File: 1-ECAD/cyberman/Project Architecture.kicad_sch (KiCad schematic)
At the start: 0 parts

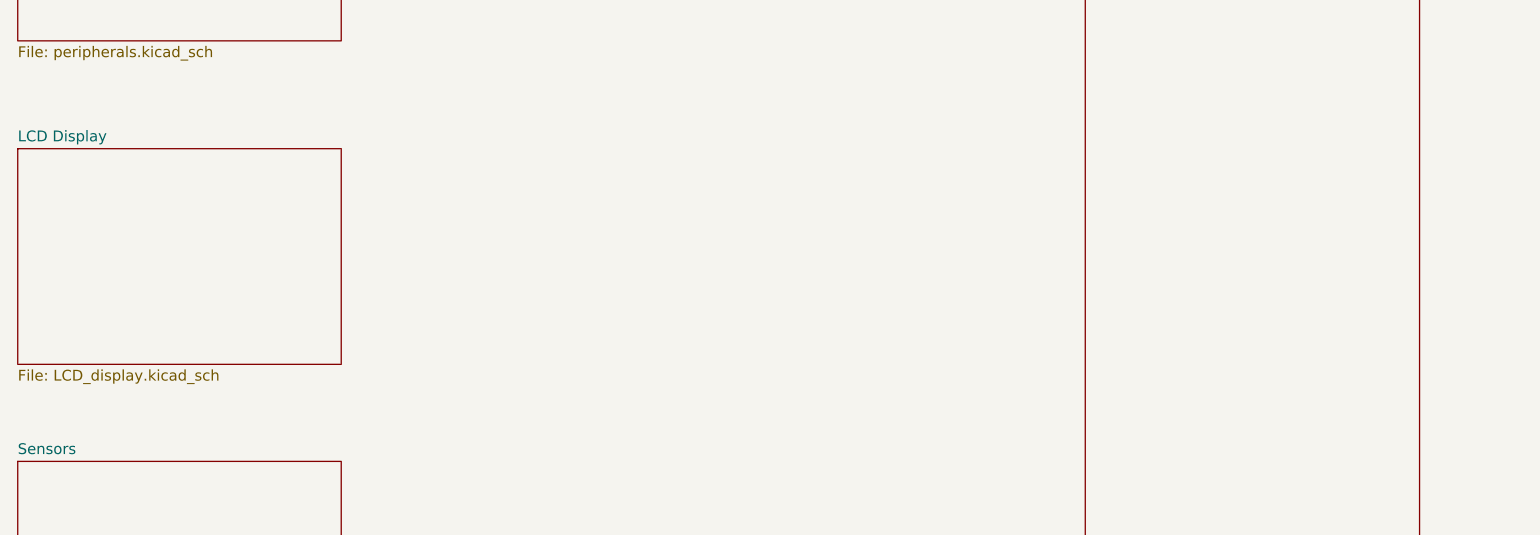
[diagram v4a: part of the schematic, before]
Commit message: add bus and display connection
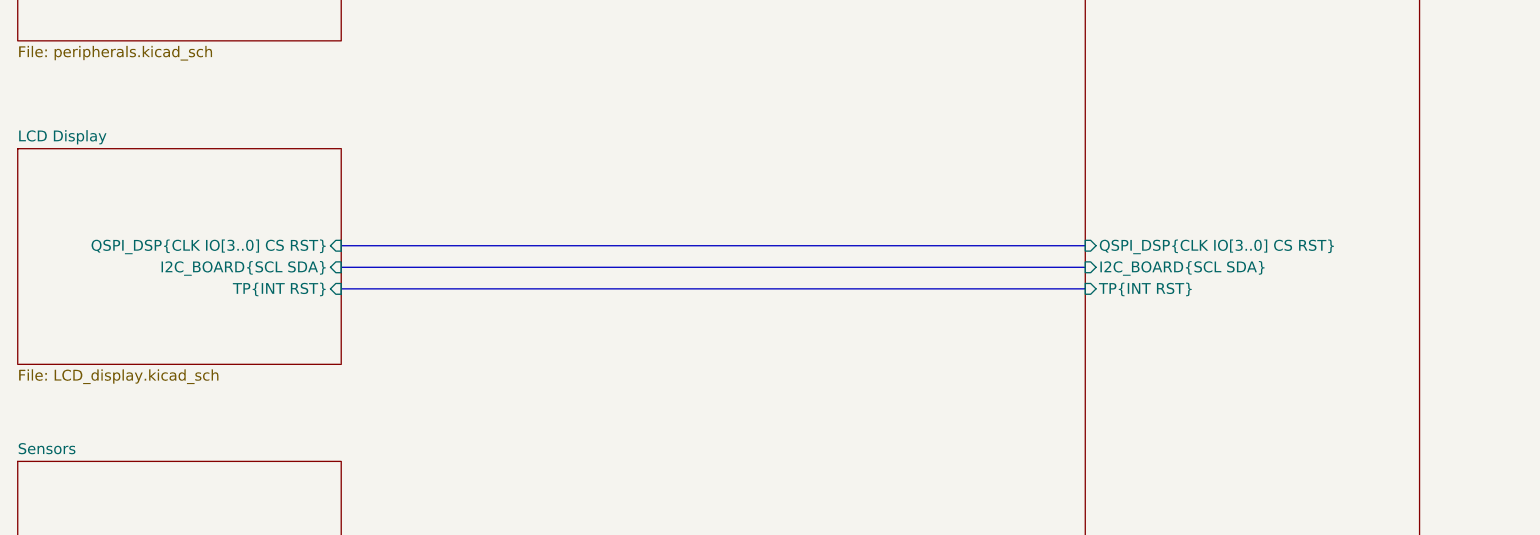
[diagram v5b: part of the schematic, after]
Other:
- sheet LCD Display ports: added I2C_BOARD{SCL SDA}, QSPI_DSP{CLK IO[3..0] CS RST}, TP{INT RST}; removed none
- sheet MCU - IOs ports: added I2C_BOARD{SCL SDA}, QSPI_DSP{CLK IO[3..0] CS RST}, TP{INT RST}; removed none
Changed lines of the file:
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@@
 		(company "${COMPANY}")
+	)
+	(bus
+		(pts
+			(xy 127 138.43) (xy 214.63 138.43)
+		)
+		(stroke
+			(width 0)
+			(type default)
+		)
+	)
+	(bus
+		(pts
+			(xy 127 140.97) (xy 214.63 140.97)
+		)
+		(stroke
+			(width 0)
+			(type default)
+		)
+	)
+	(bus
+		(pts
+			(xy 127 143.51) (xy 214.63 143.51)
+		)
+		(stroke
+			(width 0)
+			(type default)
+		)
 	)
 	(text_box "[${#}] ${TITLE}"
@@
 			)
 		)
+		(pin "QSPI_DSP{CLK IO[3..0] CS RST}" input
+			(at 127 138.43 0)
+			(effects
+				(font
+					(size 1.27 1.27)
+				)
+				(justify right)
+			)
+		)
+		(pin "TP{INT RST}" input
+			(at 127 143.51 0)
+			(effects
+				(font
+					(size 1.27 1.27)
+				)
+				(justify right)
+			)
+		)
+		(pin "I2C_BOARD{SCL SDA}" input
+			(at 127 140.97 0)
+			(effects
+				(font
+					(size 1.27 1.27)
+				)
+				(justify right)
+			)
+		)
 		(instances
 			(project "cyberman"
@@
 			)
 		)
+		(pin "TP{INT RST}" input
+			(at 214.63 143.51 180)
+			(effects
+				(font
+					(size 1.27 1.27)
+				)
+				(justify left)
+			)
+		)
+		(pin "QSPI_DSP{CLK IO[3..0] CS RST}" input
+			(at 214.63 138.43 180)
+			(effects
+				(font
+					(size 1.27 1.27)
+				)
+				(justify left)
+			)
+		)
+		(pin "I2C_BOARD{SCL SDA}" input
+			(at 214.63 140.97 180)
+			(effects
+				(font
+					(size 1.27 1.27)
+				)
+				(justify left)
+			)
+		)

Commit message: hey
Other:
- sheet LCD Display ports: added BOARD_I2C{SCL SDA}, DSP{CS RST}, QSPI{CLK IO[3..0]}; removed I2C_BOARD{SCL SDA}, QSPI_DSP{CLK IO[3..0] CS RST}
- sheet MCU - IOs ports: added BOARD_I2C{SCL SDA}, DSP{CS RST}, I2S{SCK SD WS}, QSPI{CLK IO[3..0]}, SD{CS CD}; removed I2C_BOARD{SCL SDA}, QSPI_DSP{CLK IO[3..0] CS RST}
- sheet Peripherals ports: added QSPI{CLK IO[3..0]}, SD{CS CD}; removed none
- sheet Power ports: added I2C_AUX{SCL SDA}, I2C_BOARD{SCL SDA}, PWR{PERIPH RST}; removed none
- sheet Sensors ports: added I2C_BOARD{SCL SDA}, I2S{SCK SD WS}; removed none
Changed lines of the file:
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@@
 		(company "${COMPANY}")
 	)
-	(bus
-		(pts
-			(xy 127 138.43) (xy 214.63 138.43)
-		)
-		(stroke
-			(width 0)
-			(type default)
-		)
-	)
-	(bus
-		(pts
-			(xy 127 140.97) (xy 214.63 140.97)
-		)
-		(stroke
-			(width 0)
-			(type default)
-		)
-	)
-	(bus
-		(pts
-			(xy 127 143.51) (xy 214.63 143.51)
+	(junction
+		(at 163.83 142.24)
+		(diameter 0)
+		(color 0 0 0 0)
+	)
+	(junction
+		(at 163.83 134.62)
+		(diameter 0)
+		(color 0 0 0 0)
+	)
+	(bus
+		(pts
+			(xy 127 179.07) (xy 214.63 179.07)
+		)
+		(stroke
+			(width 0)
+			(type default)
+		)
+	)
+	(bus
+		(pts
+			(xy 163.83 99.06) (xy 163.83 134.62)
+		)
+		(stroke
+			(width 0)
+			(type default)
+		)
+	)
+	(bus
+		(pts
+			(xy 127 139.7) (xy 214.63 139.7)
+		)
+		(stroke
+			(width 0)
+			(type default)
+		)
+	)
+	(bus
+		(pts
+			(xy 127 99.06) (xy 163.83 99.06)
+		)
+		(stroke
+			(width 0)
+			(type default)
+		)
+	)
+	(bus
+		(pts
+			(xy 127 134.62) (xy 163.83 134.62)
+		)
+		(stroke
+			(width 0)
+			(type default)
+		)
+	)
+	(bus
+		(pts
+			(xy 127 142.24) (xy 163.83 142.24)
+		)
+		(stroke
+			(width 0)
+			(type default)
+		)
+	)
+	(bus
+		(pts
+			(xy 127 101.6) (xy 214.63 101.6)
+		)
+		(stroke
+			(width 0)
+			(type default)
+		)
+	)
+	(bus
+		(pts
+			(xy 163.83 142.24) (xy 214.63 142.24)
+		)
+		(stroke
+			(width 0)
+			(type default)
+		)
+	)
+	(bus
+		(pts
+			(xy 163.83 134.62) (xy 214.63 134.62)
+		)
+		(stroke
+			(width 0)
+			(type default)
+		)
+	)
+	(bus
+		(pts
+			(xy 127 176.53) (xy 163.83 176.53)
+		)
+		(stroke
+			(width 0)
+			(type default)
+		)
+	)
+	(bus
+		(pts
+			(xy 163.83 142.24) (xy 163.83 176.53)
+		)
+		(stroke
+			(width 0)
+			(type default)
+		)
+	)
+	(bus
+		(pts
+			(xy 127 137.16) (xy 214.63 137.16)
 		)
 		(stroke
@@
 			)
 		)
+		(pin "I2C_BOARD{SCL SDA}" input
+			(at 127 66.04 0)
+			(effects
+				(font
+					(size 1.27 1.27)
+				)
+				(justify right)
+			)
+		)
+		(pin "I2C_AUX{SCL SDA}" input
+			(at 127 63.5 0)
+			(effects
+				(font
+					(size 1.27 1.27)
+				)
+				(justify right)
+			)
+		)
+		(pin "PWR{PERIPH RST}" input
+			(at 127 60.96 0)
+			(effects
+				(font
+					(size 1.27 1.27)
+				)
+				(justify right)
+			)
+		)
 		(instances
 			(project "cyberman"
@@
 			)
 		)
-		(pin "QSPI_DSP{CLK IO[3..0] CS RST}" input
-			(at 127 138.43 0)
-			(effects
-				(font
-					(size 1.27 1.27)
-				)
-				(justify right)
-			)
-		)
 		(pin "TP{INT RST}" input
-			(at 127 143.51 0)
-			(effects
-				(font
-					(size 1.27 1.27)
-				)
-				(justify right)
-			)
-		)
-		(pin "I2C_BOARD{SCL SDA}" input
-			(at 127 140.97 0)
+			(at 127 139.7 0)
+			(effects
+				(font
+					(size 1.27 1.27)
+				)
+				(justify right)
+			)
+		)
+		(pin "BOARD_I2C{SCL SDA}" input
+			(at 127 142.24 0)
+			(effects
+				(font
+					(size 1.27 1.27)
+				)
+				(justify right)
+			)
+		)
+		(pin "DSP{CS RST}" input
+			(at 127 137.16 0)
+			(effects
+				(font
+					(size 1.27 1.27)
+				)
+				(justify right)
+			)
+		)
+		(pin "QSPI{CLK IO[3..0]}" input
+			(at 127 134.62 0)
 			(effects
 				(font
@@
 			)
 		)
+		(pin "QSPI{CLK IO[3..0]}" input
+			(at 127 99.06 0)
+			(effects
+				(font
+					(size 1.27 1.27)
+				)
+				(justify right)
+			)
+		)
+		(pin "SD{CS CD}" input
+			(at 127 101.6 0)
+			(effects
+				(font
+					(size 1.27 1.27)
+				)
+				(justify right)
+			)
+		)
 		(instances
 			(project "cyberman"
@@
 	)
 	(sheet
-		(at 88.9 163.83)
-		(size 38.1 26.67)
+		(at 88.9 165.1)
+		(size 38.1 25.4)
 		(fields_autoplaced yes)
 		(stroke
@@
 		)
 		(property "Sheetname" "Sensors"
-			(at 88.9 163.1184 0)
+			(at 88.9 164.3884 0)
 			(effects
 				(font
@@
 				)
 				(justify left top)
+			)
+		)
+		(pin "I2C_BOARD{SCL SDA}" input
+			(at 127 176.53 0)
+			(effects
+				(font
+					(size 1.27 1.27)
+				)
+				(justify right)
+			)
+		)
+		(pin "I2S{SCK SD WS}" input
+			(at 127 179.07 0)
+			(effects
+				(font
+					(size 1.27 1.27)
+				)
+				(justify right)
 			)
 		)
@@
 			)
 		)
+		(pin "I2S{SCK SD WS}" input
+			(at 214.63 179.07 180)
+			(effects
+				(font
+					(size 1.27 1.27)
+				)
+				(justify left)
+			)
+		)
+		(pin "BOARD_I2C{SCL SDA}" input
+			(at 214.63 142.24 180)
+			(effects
+				(font
+					(size 1.27 1.27)
+				)
+				(justify left)
+			)
+		)
+		(pin "QSPI{CLK IO[3..0]}" input
+			(at 214.63 134.62 180)
+			(effects
+				(font
+					(size 1.27 1.27)
+				)
+				(justify left)
+			)
+		)
+		(pin "DSP{CS RST}" input
+			(at 214.63 137.16 180)
+			(effects
+				(font
+					(size 1.27 1.27)
+				)
+				(justify left)
+			)
+		)
 		(pin "TP{INT RST}" input
-			(at 214.63 143.51 180)
+			(at 214.63 139.7 180)
 			(effects
 				(font
@@
 			)
 		)
-		(pin "QSPI_DSP{CLK IO[3..0] CS RST}" input
-			(at 214.63 138.43 180)
-			(effects
-				(font
-					(size 1.27 1.27)
-				)
-				(justify left)
-			)
-		)
-		(pin "I2C_BOARD{SCL SDA}" input
-			(at 214.63 140.97 180)
-			(effects
-				(font
+		(pin "SD{CS CD}" input
+			(at 214.63 101.6 180)
+			(effects
+				(font

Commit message: connections
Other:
- added sheet PIC (pic.kicad_sch)
- sheet LCD Display ports: added none; removed TP{INT RST}
- sheet MCU - IOs ports: added BUTTON{LEFT TOP RIGHT BOTTOM SELECT BACK}, SD{CS CLK MOSI MISO CD}; removed SD{CS CD}, TP{INT RST}
- sheet Peripherals ports: added BUTTON{LEFT TOP RIGHT BOTTOM SELECT BACK}, SD{CS CLK MOSI MISO CD}; removed QSPI{CLK IO[3..0]}, SD{CS CD}
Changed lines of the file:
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@@
 		(color 0 0 0 0)
 	)
-	(junction
-		(at 163.83 134.62)
-		(diameter 0)
-		(color 0 0 0 0)
-	)
 	(bus
 		(pts
@@
 	(bus
 		(pts
-			(xy 163.83 99.06) (xy 163.83 134.62)
-		)
-		(stroke
-			(width 0)
-			(type default)
-		)
-	)
-	(bus
-		(pts
-			(xy 127 139.7) (xy 214.63 139.7)
-		)
-		(stroke
-			(width 0)
-			(type default)
-		)
-	)
-	(bus
-		(pts
-			(xy 127 99.06) (xy 163.83 99.06)
-		)
-		(stroke
-			(width 0)
-			(type default)
-		)
-	)
-	(bus
-		(pts
-			(xy 127 134.62) (xy 163.83 134.62)
+			(xy 127 101.6) (xy 215.9 101.6)
 		)
 		(stroke
@@
 	(bus
 		(pts
-			(xy 127 101.6) (xy 214.63 101.6)
-		)
-		(stroke
-			(width 0)
-			(type default)
-		)
-	)
-	(bus
-		(pts
 			(xy 163.83 142.24) (xy 214.63 142.24)
 		)
@@
 	(bus
 		(pts
-			(xy 163.83 134.62) (xy 214.63 134.62)
+			(xy 127 99.06) (xy 215.9 99.06)
+		)
+		(stroke
+			(width 0)
+			(type default)
+		)
+	)
+	(bus
+		(pts
+			(xy 127 134.62) (xy 214.63 134.62)
 		)
 		(stroke
@@
 	(text "Page 5"
 		(exclude_from_sim no)
-		(at 252.73 227.33 0)
+		(at 252.73 201.93 0)
 		(effects
 			(font
@@
 			)
 		)
-		(pin "TP{INT RST}" input
-			(at 127 139.7 0)
-			(effects
-				(font
-					(size 1.27 1.27)
-				)
-				(justify right)
-			)
-		)
 		(pin "BOARD_I2C{SCL SDA}" input
 			(at 127 142.24 0)
@@
 			)
 		)
-		(pin "QSPI{CLK IO[3..0]}" input
+		(pin "SD{CS CLK MOSI MISO CD}" input
 			(at 127 99.06 0)
 			(effects
@@
 			)
 		)
-		(pin "SD{CS CD}" input
+		(pin "BUTTON{LEFT TOP RIGHT BOTTOM SELECT BACK}" input
 			(at 127 101.6 0)
 			(effects
@@
 	)
 	(sheet
+		(at 215.9 215.9)
+		(size 38.1 25.4)
+		(fields_autoplaced yes)
+		(stroke
+			(width 0.1524)
+			(type solid)
+		)
+		(fill
+			(color 0 0 0 0.0000)
+		)
+		(property "Sheetname" "PIC"
+			(at 215.9 215.1884 0)
+			(effects
+				(font
+					(size 1.27 1.27)
+				)
+				(justify left bottom)
+			)
+		)
+		(property "Sheetfile" "pic.kicad_sch"
+			(at 215.9 241.8846 0)
+			(effects
+				(font
+					(size 1.27 1.27)
+				)
+				(justify left top)
+			)
+		)
+		(instances
+			(project "cyberman"
+				(path "/0650c7a8-acba-429c-9f8e-eec0baf0bc1c/fede4c36-00cc-4d3d-b71c-5243ba232202"
+					(page "11")
+				)
+			)
+		)
+	)
+	(sheet
 		(at 215.9 50.8)
 		(size 38.1 25.4)
@@
 	)
 	(sheet
-		(at 214.63 88.9)
-		(size 39.37 139.7)
+		(at 215.9 88.9)
+		(size 39.37 114.3)
 		(fields_autoplaced yes)
 		(stroke
@@
 		)
 		(property "Sheetname" "MCU - IOs"
-			(at 214.63 88.1884 0)
+			(at 215.9 88.1884 0)
 			(effects
 				(font
@@
 		)
 		(property "Sheetfile" "mcu-IOs.kicad_sch"
-			(at 214.63 229.1846 0)
+			(at 215.9 203.7846 0)
 			(effects
 				(font
@@
 		)
 		(pin "I2S{SCK SD WS}" input
-			(at 214.63 179.07 180)
+			(at 215.9 179.07 180)
 			(effects
 				(font
@@
 		)
 		(pin "BOARD_I2C{SCL SDA}" input
-			(at 214.63 142.24 180)
+			(at 215.9 142.24 180)
 			(effects
 				(font
@@
 		)
 		(pin "QSPI{CLK IO[3..0]}" input
-			(at 214.63 134.62 180)
+			(at 215.9 134.62 180)
 			(effects
 				(font
@@
 		)
 		(pin "DSP{CS RST}" input
-			(at 214.63 137.16 180)
+			(at 215.9 137.16 180)
 			(effects
 				(font
@@
 			)
 		)
-		(pin "TP{INT RST}" input
-			(at 214.63 139.7 180)
+		(pin "BUTTON{LEFT TOP RIGHT BOTTOM SELECT BACK}" input
+			(at 215.9 101.6 180)
 			(effects
 				(font
@@
 			)
 		)
-		(pin "SD{CS CD}" input
-			(at 214.63 101.6 180)
-			(effects
-				(font
+		(pin "SD{CS CLK MOSI MISO CD}" input
+			(at 215.9 99.06 180)
+			(effects
+				(font
